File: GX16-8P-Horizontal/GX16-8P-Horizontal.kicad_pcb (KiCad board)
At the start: 2 copper layers, 24.1 x 15.9 mm, 2 parts, among them J1 GX16, J2 Board Header

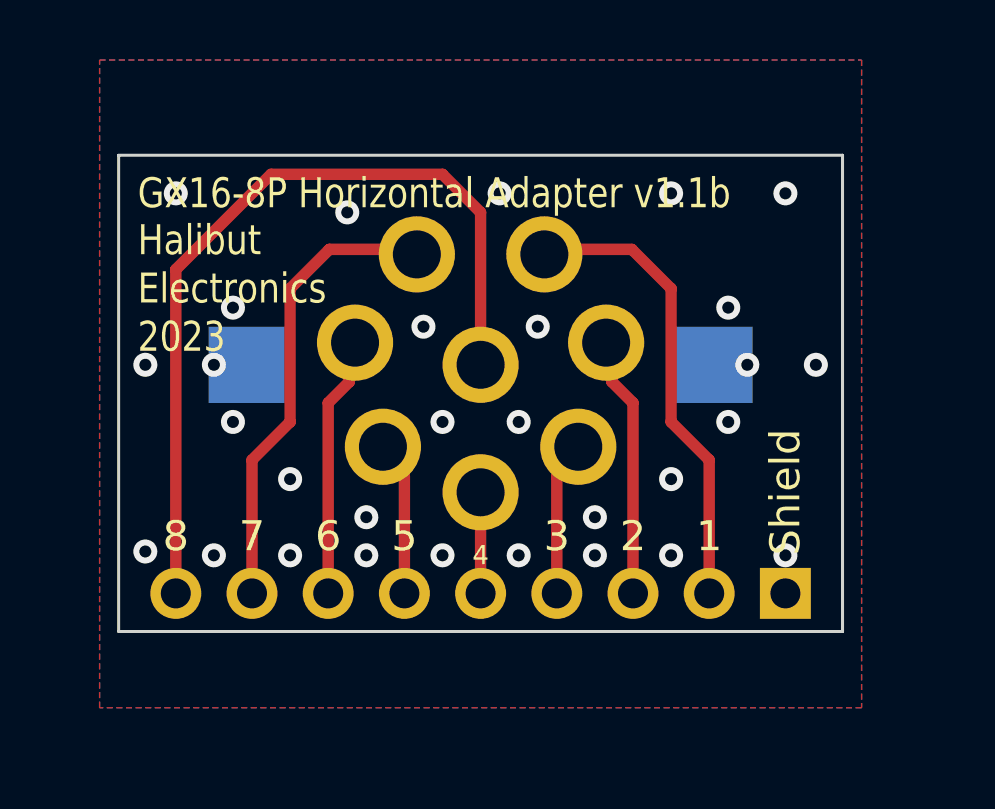
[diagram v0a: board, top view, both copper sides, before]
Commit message: https://github.com/Halibut-Electronics/HHI-Radio-Pro/issues/34 Switched from pins to card edge.
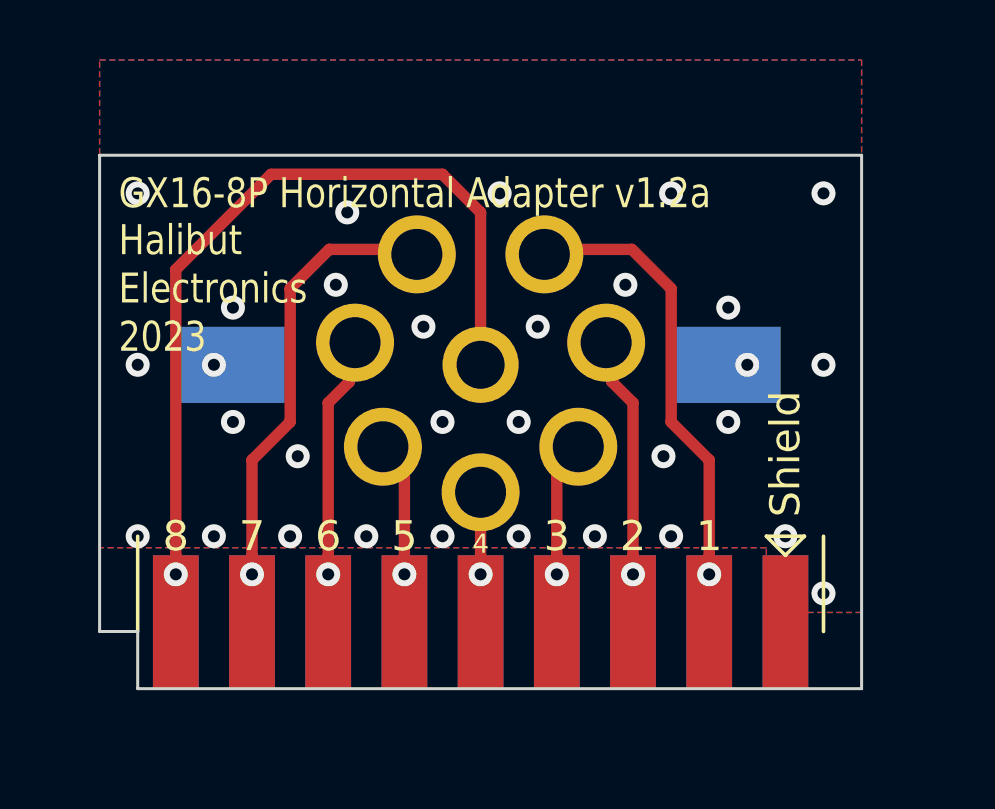
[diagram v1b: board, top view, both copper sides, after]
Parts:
- added J3: Board Header RtoL, Libraries:Conn_B2B-RA_2.54mm_ThroughPads_9pin_RtoL, F.Cu at (127.0, 72.4)
- J2: value Board Header -> Board Header LtoR; footprint Connector_PinHeader_2.54mm:PinHeader_1x09_P2.54mm_Vertical -> Libraries:Conn_B2B-RA_2.54mm_ThroughPads_9pin_LtoR
- moved J2 10.2 mm to (127.0, 72.4), turned to 180 degrees
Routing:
- net Net-(J1-Pin_8): vias 0 -> 1
- net Net-(J1-Pin_7): vias 0 -> 1
- net Net-(J1-Pin_6): vias 0 -> 1
- net Net-(J1-Pin_5): vias 0 -> 1
- net Net-(J1-Pin_4): vias 0 -> 1
- net Net-(J1-Pin_3): vias 0 -> 1
- net Net-(J1-Pin_2): vias 0 -> 1
- net Net-(J1-Pin_1): vias 0 -> 1
- net GND: vias 30 -> 31
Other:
- board size 24.1 x 15.9 mm -> 25.4 x 17.8 mm
- board text added: "GX16-8P Horizontal Adapter v1.2a"
- board text removed: "GX16-8P Horizontal Adapter v1.1b"

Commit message: https://github.com/Halibut-Electronics/HHI-User-Pro/issues/18 flip key to Pin9
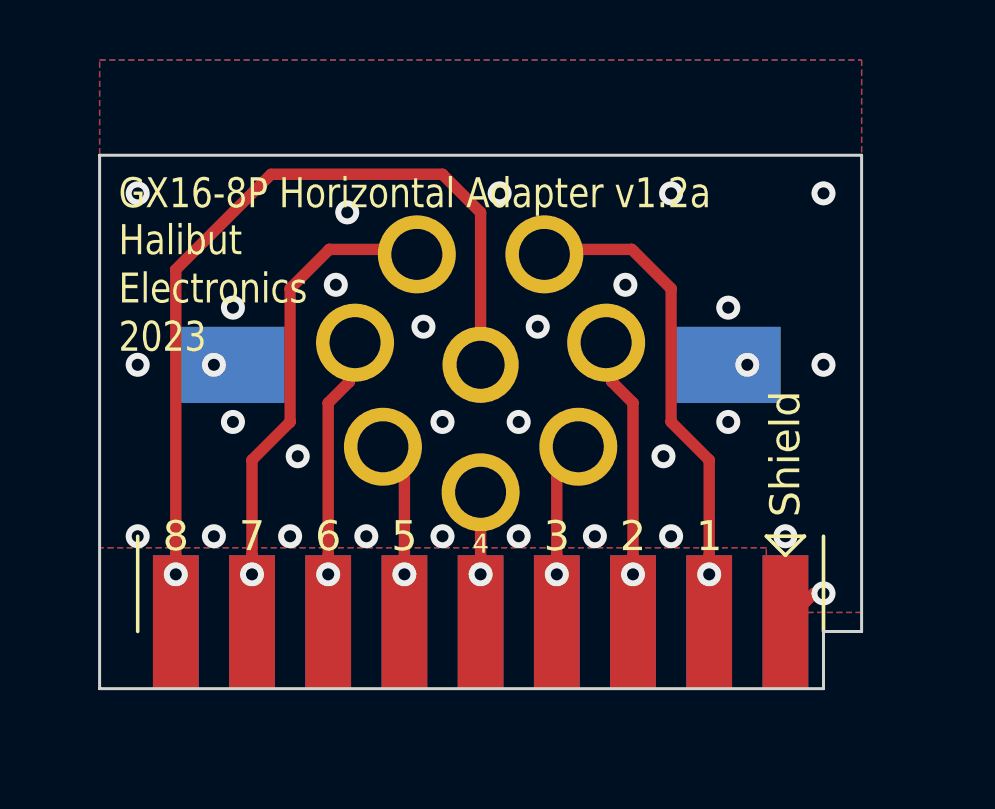
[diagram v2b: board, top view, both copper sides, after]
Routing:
- net GND: track 0.00 -> 1.66 mm
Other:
- outline, holes or cut-outs redrawn
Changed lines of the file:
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@@
       (net 9 "Net-(J1-Pin_8)") (pinfunction "Pin_9") (pintype "passive"))
   )
-  (gr_line (start 114.3 72.39) (end 114.3 56.515)
+  (gr_line (start 114.3 74.295) (end 114.3 56.515)
     (stroke (width 0.1) (type default)) (layer "Edge.Cuts"))
-  (gr_line (start 115.57 74.295) (end 115.57 72.39)
+  (gr_line (start 139.7 56.515) (end 139.7 72.39)
     (stroke (width 0.1) (type default)) (layer "Edge.Cuts"))
-  (gr_line (start 139.7 56.515) (end 139.7 74.295)
+  (gr_line (start 138.43 72.39) (end 138.43 74.295)
     (stroke (width 0.1) (type default)) (layer "Edge.Cuts"))
-  (gr_line (start 139.7 74.295) (end 115.57 74.295)
+  (gr_line (start 138.43 74.295) (end 114.3 74.295)
+    (stroke (width 0.1) (type default)) (layer "Edge.Cuts"))
+  (gr_line (start 139.7 72.39) (end 138.43 72.39)
     (stroke (width 0.1) (type default)) (layer "Edge.Cuts"))
   (gr_line (start 114.3 56.515) (end 139.7 56.515)
-    (stroke (width 0.1) (type default)) (layer "Edge.Cuts"))
-  (gr_line (start 115.57 72.39) (end 114.3 72.39)
     (stroke (width 0.1) (type default)) (layer "Edge.Cuts"))
   (gr_text "Shield" (at 137.16 68.58 90) (layer "F.SilkS")
@@
     (style (thickness 0.15) (arrow_length 1.27) (text_position_mode 0) (extension_height 0.58642) (extension_offset 0.5) keep_text_aligned)
   )
+  (segment (start 138.1125 71.12) (end 137.16 72.0725) (width 0.381) (layer "F.Cu") (net 1))
+  (segment (start 138.43 71.12) (end 138.1125 71.12) (width 0.381) (layer "F.Cu") (net 1))
   (via (at 115.57 57.785) (size 0.8) (drill 0.4) (layers "F.Cu" "B.Cu") (free) (net 1))
   (via (at 128.27 65.405) (size 0.8) (drill 0.4) (layers "F.Cu" "B.Cu") (free) (net 1))

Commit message: https://github.com/Halibut-Electronics/HHI-Radio-Pro/issues/43 Castelated the bottom edge to make soldering from the bottom easier.
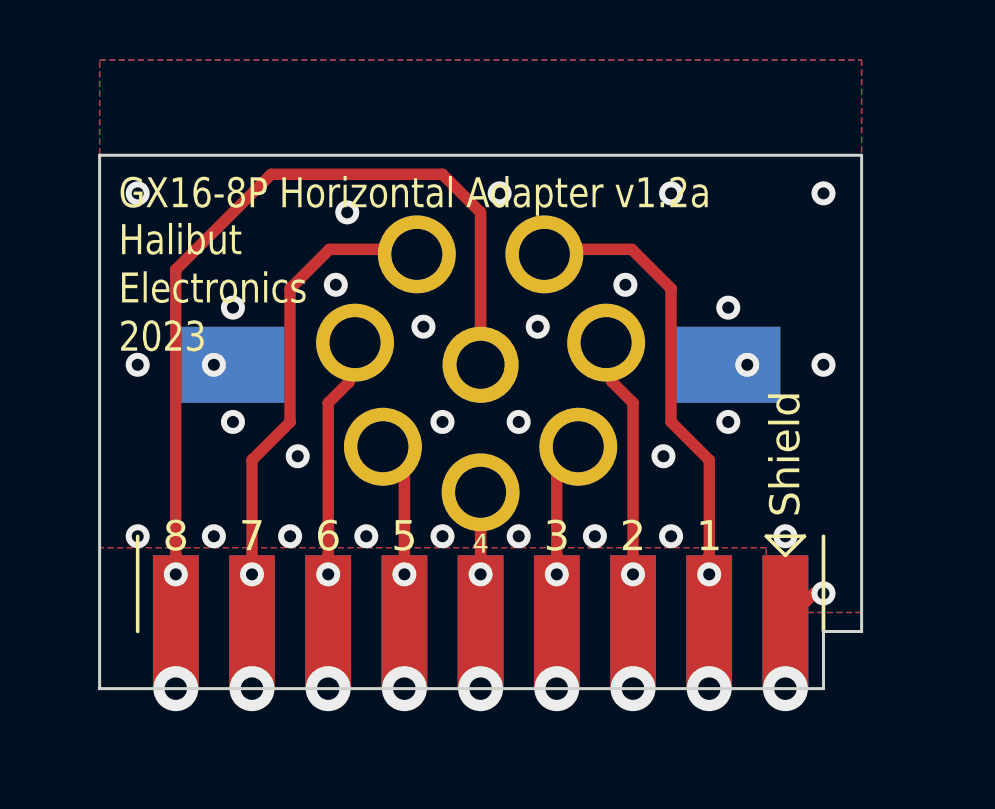
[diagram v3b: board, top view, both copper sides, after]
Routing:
- net Net-(J1-Pin_8): vias 1 -> 2
- net Net-(J1-Pin_7): vias 1 -> 2
- net Net-(J1-Pin_6): vias 1 -> 2
- net Net-(J1-Pin_5): vias 1 -> 2
- net Net-(J1-Pin_4): vias 1 -> 2
- net Net-(J1-Pin_3): vias 1 -> 2
- net Net-(J1-Pin_2): vias 1 -> 2
- net Net-(J1-Pin_1): vias 1 -> 2
- net GND: vias 31 -> 32
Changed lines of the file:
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@@
     (pts (xy 115.57 74.295) (xy 139.7 74.295))
     (height 6.985)
-    (gr_text "0.9500 in" (at 127.635 80.13) (layer "Dwgs.User")
+    (gr_text "24.1300 mm" (at 127.635 80.13) (layer "Dwgs.User")
       (effects (font (size 1 1) (thickness 0.15)))
     )
@@
     (pts (xy 115.57 74.295) (xy 127 74.295))
     (height 3.81)
-    (gr_text "0.4500 in" (at 121.285 76.955) (layer "Dwgs.User")
+    (gr_text "11.4300 mm" (at 121.285 76.955) (layer "Dwgs.User")
       (effects (font (size 1 1) (thickness 0.15)))
     )
@@
     (pts (xy 127 63.5) (xy 127 72.39))
     (height -17.145)
-    (gr_text "0.3500 in" (at 142.995 67.945 90) (layer "Dwgs.User")
+    (gr_text "8.8900 mm" (at 142.995 67.945 90) (layer "Dwgs.User")
       (effects (font (size 1 1) (thickness 0.15)))
     )
@@
   (via (at 128.905 62.23) (size 0.8) (drill 0.4) (layers "F.Cu" "B.Cu") (free) (net 1))
   (via (at 131.826 60.833) (size 0.8) (drill 0.4) (layers "F.Cu" "B.Cu") (free) (net 1))
+  (via (at 137.16 74.295) (size 1.5) (drill 0.75) (layers "F.Cu" "B.Cu") (net 1))
   (via (at 138.43 71.12) (size 0.8) (drill 0.4) (layers "F.Cu" "B.Cu") (free) (net 1))
   (via (at 125.73 65.405) (size 0.8) (drill 0.4) (layers "F.Cu" "B.Cu") (free) (net 1))
@@
   (segment (start 133.35 65.405) (end 134.62 66.675) (width 0.381) (layer "F.Cu") (net 2))
   (segment (start 129.2225 59.6519) (end 132.0419 59.6519) (width 0.381) (layer "F.Cu") (net 2))
+  (via (at 134.62 74.295) (size 1.5) (drill 0.75) (layers "F.Cu" "B.Cu") (net 2))
   (via (at 134.62 70.485) (size 0.8) (drill 0.4) (layers "F.Cu" "B.Cu") (net 2))
   (segment (start 131.37642 64.06642) (end 132.08 64.77) (width 0.381) (layer "F.Cu") (net 3))
@@
   (segment (start 132.08 69.85) (end 132.08 71.755) (width 0.381) (layer "F.Cu") (net 3))
   (segment (start 131.37642 62.72784) (end 131.37642 64.06642) (width 0.381) (layer "F.Cu") (net 3))
+  (via (at 132.08 74.295) (size 1.5) (drill 0.75) (layers "F.Cu" "B.Cu") (net 3))
   (via (at 132.08 70.485) (size 0.8) (drill 0.4) (layers "F.Cu" "B.Cu") (net 3))
   (segment (start 129.54 69.85) (end 129.54 67.2211) (width 0.381) (layer "F.Cu") (net 4))
@@
   (segment (start 129.54 67.2211) (end 130.4036 66.3575) (width 0.381) (layer "F.Cu") (net 4))
   (via (at 129.54 70.485) (size 0.8) (drill 0.4) (layers "F.Cu" "B.Cu") (net 4))
+  (via (at 129.54 74.295) (size 1.5) (drill 0.75) (layers "F.Cu" "B.Cu") (net 4))
   (segment (start 127 67.945) (end 127 69.85) (width 0.381) (layer "F.Cu") (net 5))
   (segment (start 127 69.85) (end 127 71.755) (width 0.381) (layer "F.Cu") (net 5))
+  (via (at 127 74.295) (size 1.5) (drill 0.75) (layers "F.Cu" "B.Cu") (net 5))
   (via (at 127 70.485) (size 0.8) (drill 0.4) (layers "F.Cu" "B.Cu") (net 5))
   (segment (start 124.46 69.85) (end 124.46 67.2211) (width 0.381) (layer "F.Cu") (net 6))
@@
   (segment (start 124.46 71.755) (end 124.46 69.85) (width 0.381) (layer "F.Cu") (net 6))
   (via (at 124.46 70.485) (size 0.8) (drill 0.4) (layers "F.Cu" "B.Cu") (net 6))
+  (via (at 124.46 74.295) (size 1.5) (drill 0.75) (layers "F.Cu" "B.Cu") (net 6))
   (segment (start 121.92 64.77) (end 121.92 69.85) (width 0.381) (layer "F.Cu") (net 7))
   (segment (start 122.62358 62.72784) (end 122.62358 64.06642) (width 0.381) (layer "F.Cu") (net 7))
@@
   (segment (start 122.62358 64.06642) (end 121.92 64.77) (width 0.381) (layer "F.Cu") (net 7))
   (via (at 121.92 70.485) (size 0.8) (drill 0.4) (layers "F.Cu" "B.Cu") (net 7))
+  (via (at 121.92 74.295) (size 1.5) (drill 0.75) (layers "F.Cu" "B.Cu") (net 7))
   (segment (start 124.7775 59.6519) (end 121.9581 59.6519) (width 0.381) (layer "F.Cu") (net 8))
   (segment (start 120.65 60.96) (end 120.65 65.405) (width 0.381) (layer "F.Cu") (net 8))
@@
   (segment (start 121.9581 59.6519) (end 120.65 60.96) (width 0.381) (layer "F.Cu") (net 8))
   (via (at 119.38 70.485) (size 0.8) (drill 0.4) (layers "F.Cu" "B.Cu") (net 8))
+  (via (at 119.38 74.295) (size 1.5) (drill 0.75) (layers "F.Cu" "B.Cu") (net 8))
   (segment (start 116.84 60.325) (end 116.84 69.85) (width 0.381) (layer "F.Cu") (net 9))
   (segment (start 120.015 57.15) (end 116.84 60.325) (width 0.381) (layer "F.Cu") (net 9))
@@
   (segment (start 116.84 69.85) (end 116.84 71.755) (width 0.381) (layer "F.Cu") (net 9))
   (segment (start 127 58.42) (end 125.73 57.15) (width 0.381) (layer "F.Cu") (net 9))
+  (via (at 116.84 74.295) (size 1.5) (drill 0.75) (layers "F.Cu" "B.Cu") (net 9))
   (via (at 116.84 70.485) (size 0.8) (drill 0.4) (layers "F.Cu" "B.Cu") (net 9))
   (zone (net 1) (net_name "GND") (layers "F&B.Cu") (hatch edge 0.508)

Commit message: https://github.com/Halibut-Electronics/HHI-Radio-Pro/issues/42 As sent to Synergetics
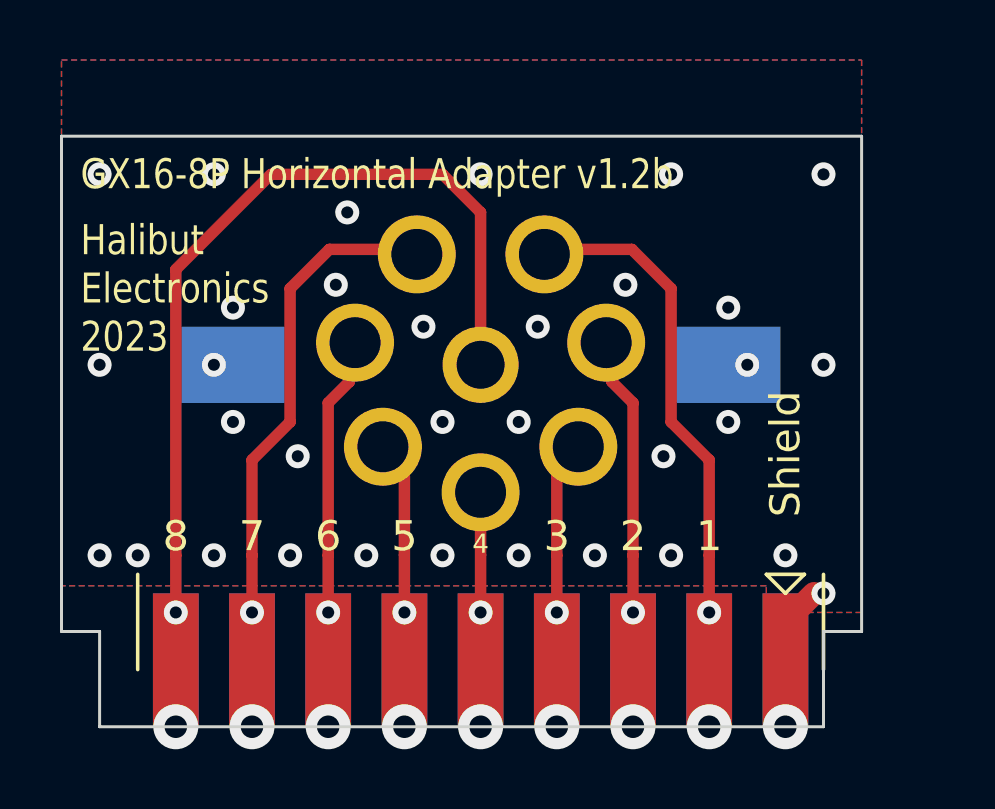
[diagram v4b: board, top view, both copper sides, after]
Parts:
- moved J2 1.27 mm to (127.0, 73.7)
- moved J3 1.27 mm to (127.0, 73.7)
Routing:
- net GND: vias 32 -> 34
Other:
- board size 25.4 x 17.8 mm -> 26.7 x 19.7 mm
- board text added: "GX16-8P Horizontal Adapter v1.2b"
- board text removed: "GX16-8P Horizontal Adapter v1.2a"
